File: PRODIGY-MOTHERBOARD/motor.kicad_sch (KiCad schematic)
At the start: 4 parts, among them U5 DRV8870DDA

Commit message: schematic v0.2 finalized
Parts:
- renumbered C33 to C32, C34 to C33
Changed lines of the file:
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@@
 		(dnp no)
 		(fields_autoplaced yes)
-		(property "Reference" "#PWR065"
+		(property "Reference" "#PWR068"
 			(at 120.65 77.47 0)
 			(effects
@@
 			(project "PRODIGY-MOTHERBOARD"
 				(path "/f1c25860-8989-4190-bd24-2491d23ca7d9/68c611b4-6626-4f5e-8db6-2b7527a0fa95"
-					(reference "#PWR065")
+					(reference "#PWR068")
 					(unit 1)
 				)
@@
 		(dnp no)
 		(fields_autoplaced yes)
-		(property "Reference" "#PWR068"
+		(property "Reference" "#PWR071"
 			(at 146.05 114.3 0)
 			(effects
@@
 			(project "PRODIGY-MOTHERBOARD"
 				(path "/f1c25860-8989-4190-bd24-2491d23ca7d9/68c611b4-6626-4f5e-8db6-2b7527a0fa95"
-					(reference "#PWR068")
+					(reference "#PWR071")
 					(unit 1)
 				)
@@
 		(dnp no)
 		(fields_autoplaced yes)
-		(property "Reference" "C33"
+		(property "Reference" "C32"
 			(at 124.46 77.8509 0)
 			(effects
@@
 			(project "PRODIGY-MOTHERBOARD"
 				(path "/f1c25860-8989-4190-bd24-2491d23ca7d9/68c611b4-6626-4f5e-8db6-2b7527a0fa95"
-					(reference "C33")
+					(reference "C32")
 					(unit 1)
 				)
@@
 		(dnp no)
 		(fields_autoplaced yes)
-		(property "Reference" "C34"
+		(property "Reference" "C33"
 			(at 138.43 78.7399 0)
 			(effects
@@
 			(project "PRODIGY-MOTHERBOARD"
 				(path "/f1c25860-8989-4190-bd24-2491d23ca7d9/68c611b4-6626-4f5e-8db6-2b7527a0fa95"
-					(reference "C34")
+					(reference "C33")
 					(unit 1)
 				)
@@
 		(dnp no)
 		(fields_autoplaced yes)
-		(property "Reference" "#PWR066"
+		(property "Reference" "#PWR069"
 			(at 123.19 102.87 0)
 			(effects
@@
 			(project "PRODIGY-MOTHERBOARD"
 				(path "/f1c25860-8989-4190-bd24-2491d23ca7d9/68c611b4-6626-4f5e-8db6-2b7527a0fa95"
-					(reference "#PWR066")
+					(reference "#PWR069")
 					(unit 1)
 				)
@@
 		(dnp no)
 		(fields_autoplaced yes)
-		(property "Reference" "#PWR067"
+		(property "Reference" "#PWR070"
 			(at 134.62 90.17 0)
 			(effects
@@
 			(project "PRODIGY-MOTHERBOARD"
 				(path "/f1c25860-8989-4190-bd24-2491d23ca7d9/68c611b4-6626-4f5e-8db6-2b7527a0fa95"
-					(reference "#PWR067")
-					(unit 1)
-				)
+					(reference "#PWR070")
+					(unit 1)
+				)

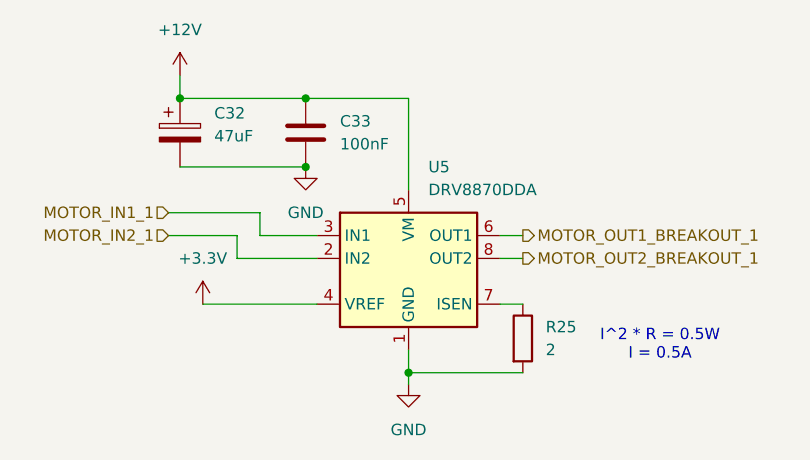
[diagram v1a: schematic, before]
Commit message: Motherboard footprints assigned.
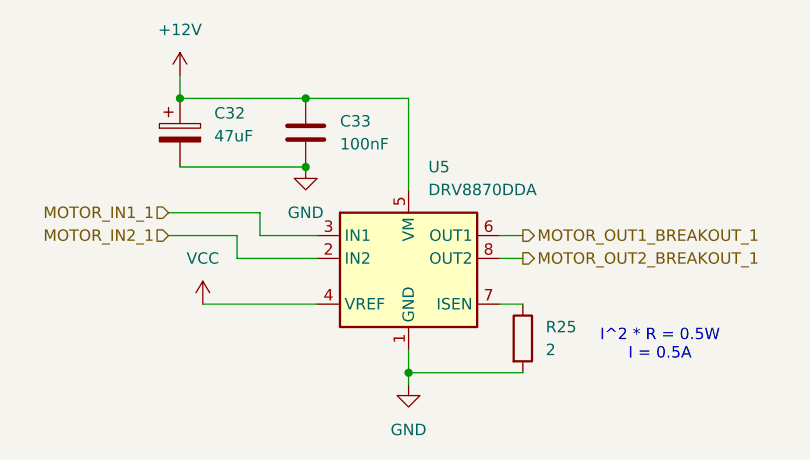
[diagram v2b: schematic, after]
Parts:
- C32: footprint Capacitor_SMD:CP_Elec_6.3x5.8 -> Capacitor_SMD:C_1210_3225Metric
- C33: footprint (none) -> Capacitor_SMD:C_0603_1608Metric
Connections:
- net +3.3V renamed VCC
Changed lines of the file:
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@@
+			)
+		)
+		(property "MOUSER" ""
+			(at 158.75 102.87 0)
+			(effects
+				(font
+					(size 1.27 1.27)
+				)
+				(hide yes)
+			)
+		)
+		(property "Sim.Type" ""
+			(at 158.75 102.87 0)
+			(effects
+				(font
+					(size 1.27 1.27)
+				)
+				(hide yes)
+			)
+		)
+		(property "TME" ""
+			(at 158.75 102.87 0)
+			(effects
+				(font
+					(size 1.27 1.27)
+				)
+				(hide yes)
 			)
 		)
@@
 			)
 		)
-		(property "Footprint" "Capacitor_SMD:CP_Elec_6.3x5.8"
+		(property "Footprint" "Capacitor_SMD:C_1210_3225Metric"
 			(at 121.6152 83.82 0)
 			(effects
@@
 		)
 		(property "Description" ""
+			(at 120.65 80.01 0)
+			(effects
+				(font
+					(size 1.27 1.27)
+				)
+				(hide yes)
+			)
+		)
+		(property "MOUSER" ""
+			(at 120.65 80.01 0)
+			(effects
+				(font
+					(size 1.27 1.27)
+				)
+				(hide yes)
+			)
+		)
+		(property "Sim.Type" ""
+			(at 120.65 80.01 0)
+			(effects
+				(font
+					(size 1.27 1.27)
+				)
+				(hide yes)
+			)
+		)
+		(property "TME" ""
 			(at 120.65 80.01 0)
 			(effects
@@
 			)
 		)
-		(property "Footprint" ""
+		(property "Footprint" "Capacitor_SMD:C_0603_1608Metric"
 			(at 135.5852 83.82 0)
 			(effects
@@
 			)
 		)
+		(property "MOUSER" ""
+			(at 134.62 80.01 0)
+			(effects
+				(font
+					(size 1.27 1.27)
+				)
+				(hide yes)
+			)
+		)
+		(property "Sim.Type" ""
+			(at 134.62 80.01 0)
+			(effects
+				(font
+					(size 1.27 1.27)
+				)
+				(hide yes)
+			)
+		)
+		(property "TME" ""
+			(at 134.62 80.01 0)
+			(effects
+				(font
+					(size 1.27 1.27)
+				)
+				(hide yes)
+			)
+		)
 		(pin "1"
 		)
@@
 				(path "/f1c25860-8989-4190-bd24-2491d23ca7d9/68c611b4-6626-4f5e-8db6-2b7527a0fa95"
 					(reference "C33")
-					(unit 1)
-				)
-			)
-		)
-	)
-	(symbol
-		(lib_id "power:+3.3V")
-		(at 123.19 99.06 0)
-		(unit 1)
-		(exclude_from_sim no)
-		(in_bom yes)
-		(on_board yes)
-		(dnp no)
-		(fields_autoplaced yes)
-		(property "Reference" "#PWR069"
-			(at 123.19 102.87 0)
-			(effects
-				(font
-					(size 1.27 1.27)
-				)
-				(hide yes)
-			)
-		)
-		(property "Value" "+3.3V"
-			(at 123.19 93.98 0)
-			(effects
-				(font
-					(size 1.27 1.27)
-				)
-			)
-		)
-		(property "Footprint" ""
-			(at 123.19 99.06 0)
-			(effects
-				(font
-					(size 1.27 1.27)
-				)
-				(hide yes)
-			)
-		)
-		(property "Datasheet" ""
-			(at 123.19 99.06 0)
-			(effects
-				(font
-					(size 1.27 1.27)
-				)
-				(hide yes)
-			)
-		)
-		(property "Description" "Power symbol creates a global label with name \"+3.3V\""
-			(at 123.19 99.06 0)
-			(effects
-				(font
-					(size 1.27 1.27)
-				)
-				(hide yes)
-			)
-		)
-		(pin "1"
-		)
-		(instances
-			(project "PRODIGY-MOTHERBOARD"
-				(path "/f1c25860-8989-4190-bd24-2491d23ca7d9/68c611b4-6626-4f5e-8db6-2b7527a0fa95"
-					(reference "#PWR069")
 					(unit 1)
 				)
@@
 			)
 		)
+		(property "MOUSER" ""
+			(at 146.05 93.98 0)
+			(effects
+				(font
+					(size 1.27 1.27)
+				)
+				(hide yes)
+			)
+		)
+		(property "Sim.Type" ""
+			(at 146.05 93.98 0)
+			(effects
+				(font
+					(size 1.27 1.27)
+				)
+				(hide yes)
+			)
+		)
+		(property "TME" ""
+			(at 146.05 93.98 0)
+			(effects
+				(font
+					(size 1.27 1.27)
+				)
+				(hide yes)
+			)
+		)
 		(pin "1"
 		)
@@
 					(unit 1)
 				)
+			)
+		)
+	)
+	(symbol
+		(lib_id "power:VCC")
+		(at 123.19 99.06 0)
+		(unit 1)
+		(exclude_from_sim no)
+		(in_bom yes)
+		(on_board yes)
+		(dnp no)
+		(fields_autoplaced yes)
+		(property "Reference" "#PWR069"
+			(at 123.19 102.87 0)
+			(effects
+				(font
+					(size 1.27 1.27)
+				)
+				(hide yes)
+			)
+		)
+		(property "Value" "VCC"
+			(at 123.19 93.98 0)
+			(effects
+				(font
+					(size 1.27 1.27)
+				)
+			)
+		)
+		(property "Footprint" ""
+			(at 123.19 99.06 0)
+			(effects
+				(font
+					(size 1.27 1.27)
+				)
+				(hide yes)
+			)
+		)
+		(property "Datasheet" ""
+			(at 123.19 99.06 0)
+			(effects
+				(font
+					(size 1.27 1.27)
+				)
+				(hide yes)
+			)
+		)
+		(property "Description" "Power symbol creates a global label with name \"VCC\""
+			(at 123.19 99.06 0)
+			(effects
+				(font
+					(size 1.27 1.27)
+				)
+				(hide yes)
+			)
+		)
+		(pin "1"
+		)
+		(instances
+			(project "PRODIGY-MOTHERBOARD"
+				(path "/f1c25860-8989-4190-bd24-2491d23ca7d9/68c611b4-6626-4f5e-8db6-2b7527a0fa95"
+					(reference "#PWR069")
+					(unit 1)
+				)

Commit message: finished motherboard bom and updated footprints
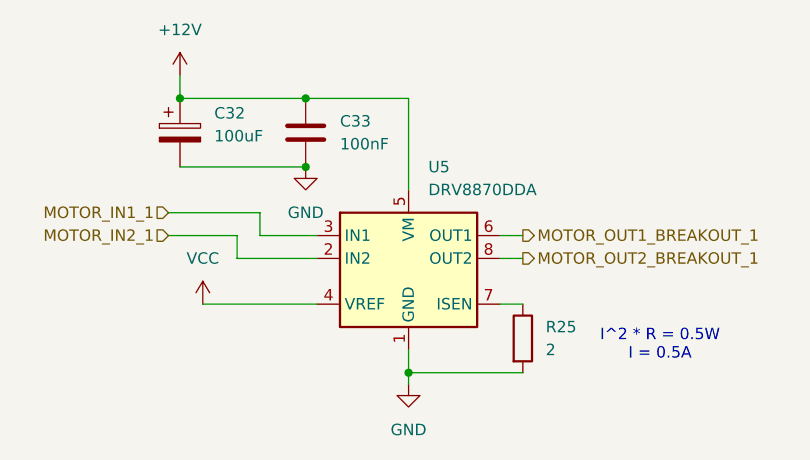
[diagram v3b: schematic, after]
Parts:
- C32: value 47uF -> 100uF; footprint Capacitor_SMD:C_1210_3225Metric -> Capacitor_SMD:CP_Elec_6.3x7.7; TME (none) -> EEEFPV101XAP
- C33: TME (none) -> CL10B104KB8NNNC
- R25: TME (none) -> SWR2512-2R-5%
- U5: TME (none) -> DRV8870DDAR
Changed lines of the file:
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@@
 			)
 		)
-		(property "TME" ""
+		(property "TME" "SWR2512-2R-5%"
 			(at 158.75 102.87 0)
 			(effects
@@
 			)
 		)
-		(property "Value" "47uF"
+		(property "Value" "100uF"
 			(at 124.46 80.3909 0)
 			(effects
@@
 			)
 		)
-		(property "Footprint" "Capacitor_SMD:C_1210_3225Metric"
+		(property "Footprint" "Capacitor_SMD:CP_Elec_6.3x7.7"
 			(at 121.6152 83.82 0)
 			(effects
@@
 			)
 		)
-		(property "TME" ""
+		(property "TME" "EEEFPV101XAP"
 			(at 120.65 80.01 0)
 			(effects
@@
 			)
 		)
-		(property "TME" ""
+		(property "TME" "CL10B104KB8NNNC  "
 			(at 134.62 80.01 0)
 			(effects
@@
 			)
 		)
-		(property "TME" ""
+		(property "TME" "DRV8870DDAR"
 			(at 146.05 93.98 0)
 			(effects
